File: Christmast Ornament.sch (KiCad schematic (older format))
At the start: 37 parts, among them J1 USB_OTG, J2 CONN_01X06, Q1 8205A, Q2 SI2302, SW1 SW_Push, SW2 SW_Push, U1 TP4056, U10 WS2812b, U2 HT7833, U3 DW01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

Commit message: Buzzer circuit and test points
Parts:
- added JP1: Jumper_NC_Dual, symbol Jumper_NC_Dual
- added Q3: BC817, TO_SOT_Packages_SMD:SOT-23, symbol BC817-40
- added R11: 470, Resistors_SMD:R_0805_HandSoldering, symbol R
- added R12, R13: 10K, Resistors_SMD:R_0805_HandSoldering, symbol R
- added TP1, TP2, TP3, TP4: TEST, Measurement_Points:Measurement_Point_Square-SMD-Pad_Small, symbol TEST
- D3: renamed from D?; footprint (none) -> Diodes_SMD:D_SMA_Handsoldering
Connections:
- net +3V3: now also JP1.1; no longer BZ1.1 (-), D3.1 (K)
- net BAT+: now also JP1.3, TP2.1
- net BAT-: now also TP4.1
- net Buzzer: now also R11.2
- net GND: now also Q3.2 (E), R12.2, R13.2, TP3.1
- net PIX_ON: now also R13.1
- net VCC: now also TP1.1
- net at BZ1.2 (+), D3.2 (A): now also Q3.3 (C)
- new net: BZ1.1 (-), D3.1 (K), JP1.2
- new net: Q3.1 (B), R11.1, R12.1
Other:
- note removed: "AÑADIR PUNTOS DE TEST"
- note removed: "Añadir puntos de test para conectar a bat+ o a 3.3v"
- note removed: "Revisar circuito para el zumbador.\n¿Añadir transistor, diodo, resistencia?"
- moved on the sheet: BZ1, C3, C6, D3, J2, Q2, R1, R5, R6, U10, U3, U4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

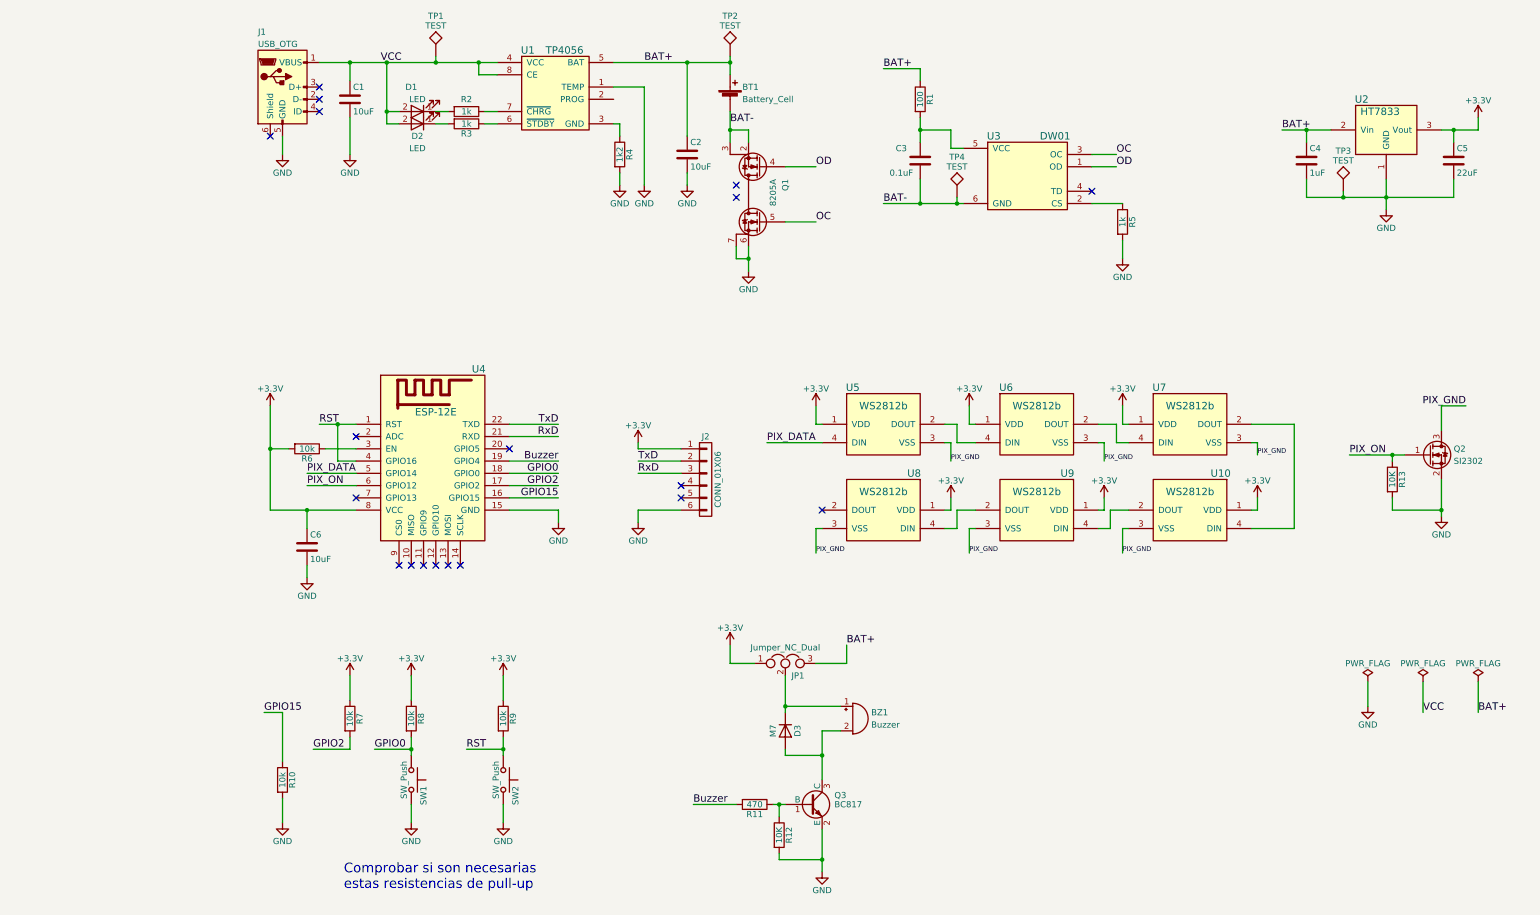
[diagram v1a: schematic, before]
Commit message: First attempt to distribute components
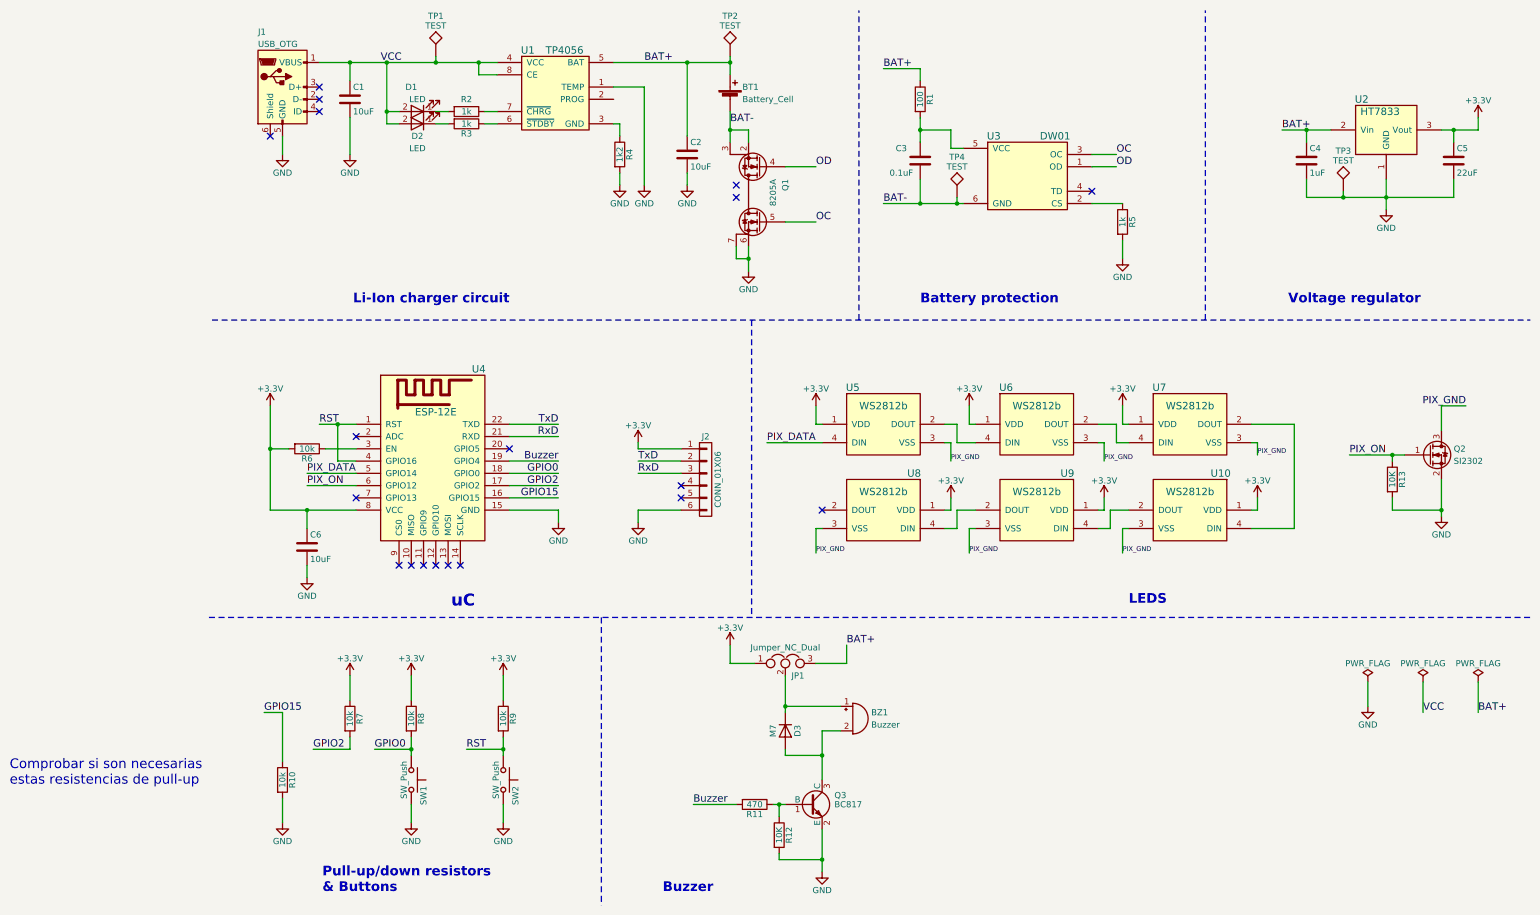
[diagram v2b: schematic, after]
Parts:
- BT1: footprint (none) -> MisModulos:18650_SMD_Case
- BZ1: footprint (none) -> MisModulos:Buzzer_8.5x8.5mm
- JP1: footprint (none) -> MisModulos:Jumper_2-NC
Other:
- note added: "Battery protection"
- note added: "Buzzer"
- note added: "LEDS"
- note added: "Li-Ion charger circuit"
- note added: "Pull-up/down resistors\n& Buttons"
- note added: "Voltage regulator"
- note added: "uC"
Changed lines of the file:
@@
 F 0 "BT1" H 4800 1300 50  0000 L CNN
 F 1 "Battery_Cell" H 4800 1200 50  0000 L CNN
-F 2 "" V 4700 1260 50  0001 C CNN
+F 2 "MisModulos:18650_SMD_Case" V 4700 1260 50  0001 C CNN
 F 3 "" V 4700 1260 50  0001 C CNN
 	1    4700 1200
@@
 F 0 "BZ1" H 5850 6300 50  0000 L CNN
 F 1 "Buzzer" H 5850 6200 50  0000 L CNN
-F 2 "" V 5675 6350 50  0001 C CNN
+F 2 "MisModulos:Buzzer_8.5x8.5mm" V 5675 6350 50  0001 C CNN
 F 3 "" V 5675 6350 50  0001 C CNN
 	1    5700 6250
@@
 	5150 6550 5450 6550
 Connection ~ 5450 6550
-Text Notes 1550 7650 0    79   ~ 0
+Text Notes -1175 6800 0    79   ~ 0
 Comprobar si son necesarias \nestas resistencias de pull-up
 $Comp
@@
 F 0 "JP1" H 5200 5700 50  0000 L CNN
 F 1 "Jumper_NC_Dual" H 5150 5900 50  0000 C BNN
-F 2 "" H 5150 5800 50  0001 C CNN
+F 2 "MisModulos:Jumper_2-NC" H 5150 5800 50  0001 C CNN
 F 3 "" H 5150 5800 50  0001 C CNN
 	1    5150 5800
@@
 	9700 1950 9700 2000
 Connection ~ 9700 2000
+Wire Notes Line
+	475  3000 11225 3000
+Wire Notes Line
+	5750 3000 5750 475
+Wire Notes Line
+	8575 3000 8575 475
+Wire Notes Line
+	450  5425 11225 5425
+Wire Notes Line
+	4875 3000 4875 5425
+Wire Notes Line
+	3650 5425 3650 7775
+Text Notes 1625 2875 0    79   ~ 16
+Li-Ion charger circuit
+Text Notes 6250 2875 0    79   ~ 16
+Battery protection
+Text Notes 9250 2875 0    79   ~ 16
+Voltage regulator
+Text Notes 7950 5325 0    79   ~ 16
+LEDS
+Text Notes 2425 5350 0    98   ~ 20
+uC
+Text Notes 4150 7675 0    79   ~ 16
+Buzzer
+Text Notes 1375 7675 0    79   ~ 16
+Pull-up/down resistors\n& Buttons
 $EndSCHEMATC

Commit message: PCB routed
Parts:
- added TP5, TP6: TEST, Measurement_Points:Measurement_Point_Square-SMD-Pad_Small, symbol TEST
- R4: value 1k2 -> 2k7
- renumbered U8 to U10, U10 to U8
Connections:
- net +3V3: now also J2.2 (P2), TP5.1; no longer J2.1 (P1)
- net GND: now also J2.1 (P1), TP6.1; no longer J2.6 (P6)
- net RxD: now also J2.5 (P5); no longer J2.3 (P3)
- net TxD: now also J2.3 (P3); no longer J2.2 (P2)

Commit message: PCB designed and gerbers
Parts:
- added C10, C11, C12, C7, C8, C9: 0.1uF, Capacitors_SMD:C_0805_HandSoldering, symbol C
- C5: value 22uF -> 2.2uF
- TP1: value TEST -> VCC
- TP2: renamed from TP6; value TEST -> GND
- TP3: renamed from TP2; value TEST -> BAT+
- TP4: value TEST -> BAT-
- TP5: value TEST -> 3V3
- TP6: renamed from TP3; value TEST -> GND
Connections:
- net +3V3: now also C10.1, C11.1, C12.1, C7.1, C8.1, C9.1
- net PIX_GND: now also C10.2, C11.2, C12.2, C7.2, C8.2, C9.2
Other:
- moved on the sheet: Q2, R13, U10, U5, U6, U7, U8, U9

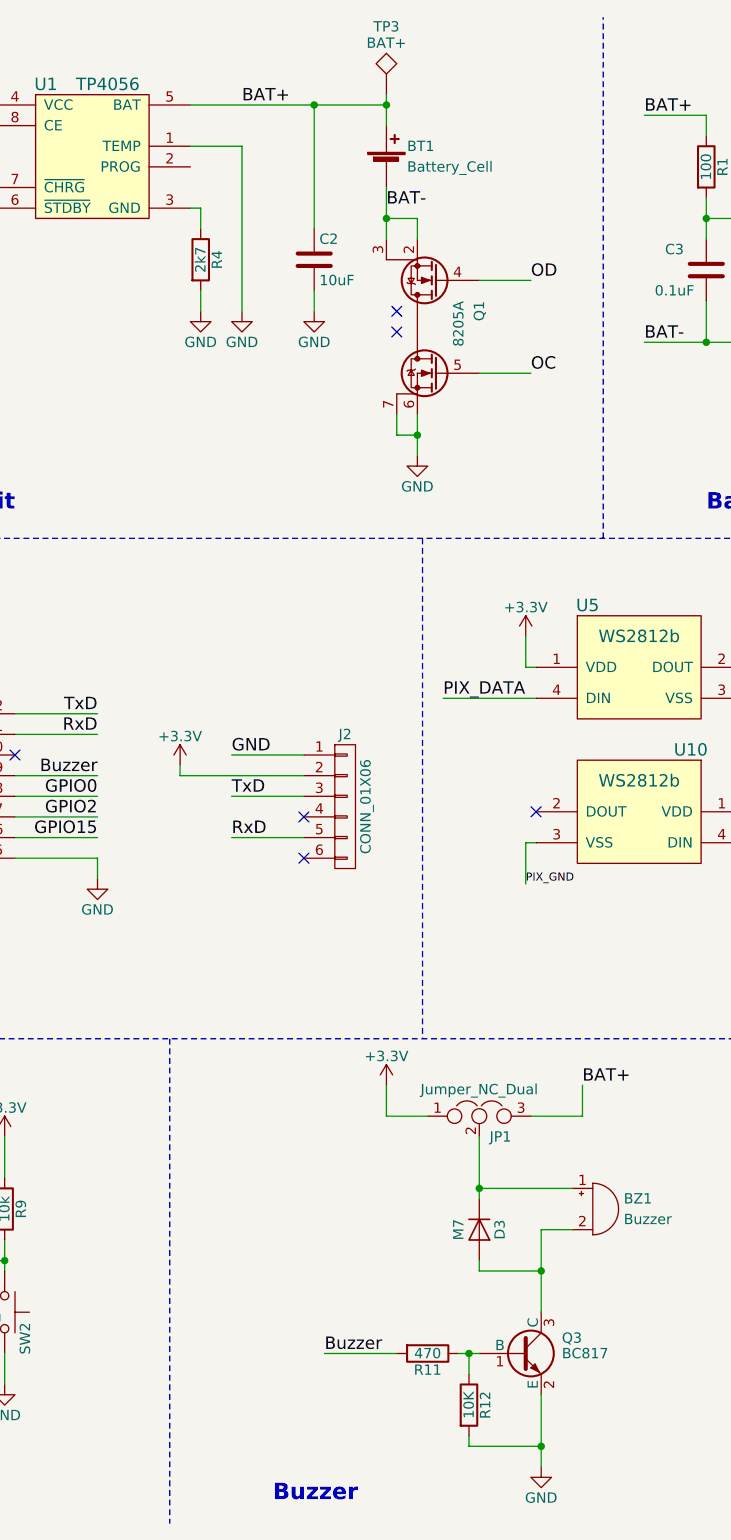
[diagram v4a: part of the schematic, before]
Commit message: TP4056 ground connection fixed
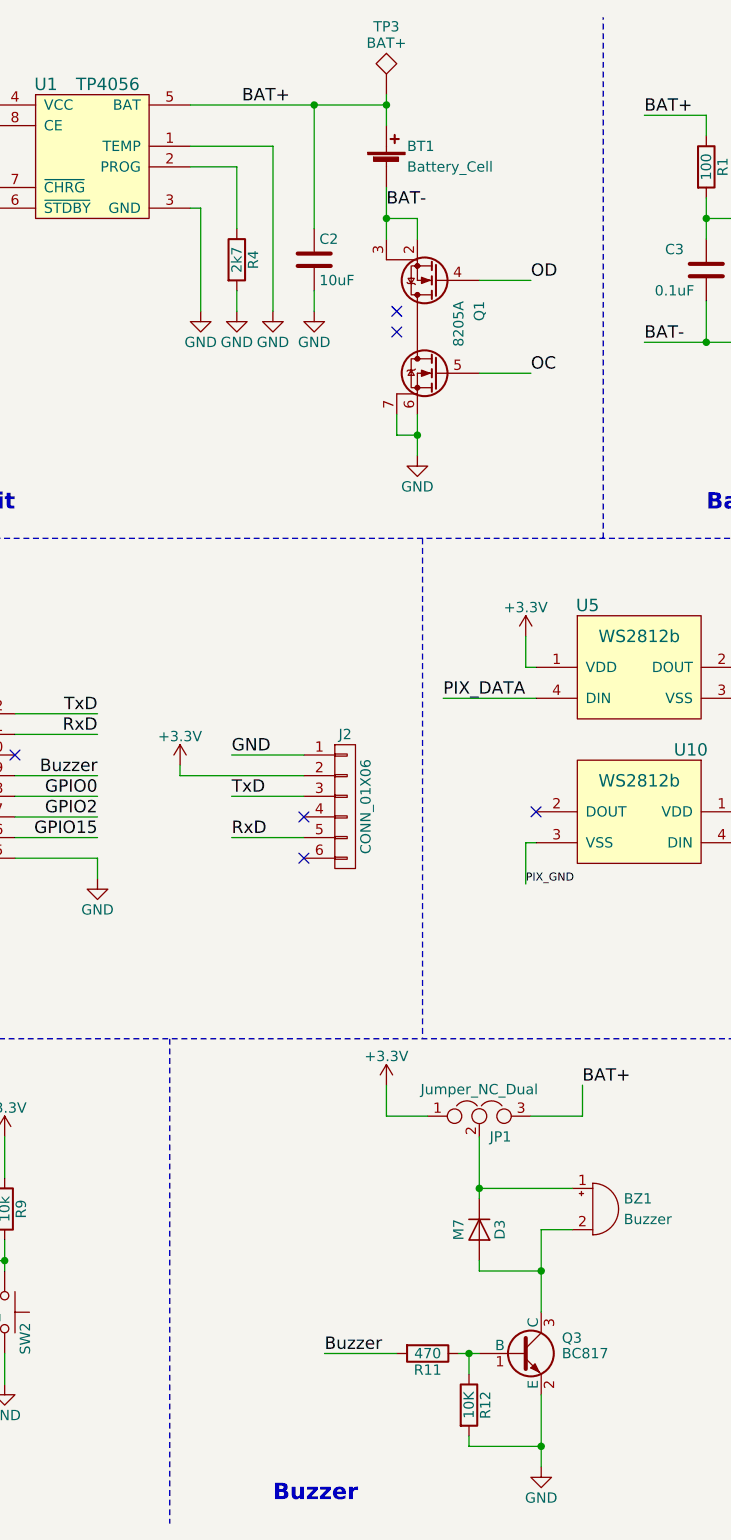
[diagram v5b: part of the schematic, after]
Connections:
- net GND: now also U1.3 (GND)
- net at U1.2 (PROG): now also R4.1
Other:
- moved on the sheet: R4
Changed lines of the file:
@@
 L GND #PWR01
 U 1 1 5AE440E5
-P 3800 1900
-F 0 "#PWR01" H 3800 1650 50  0001 C CNN
-F 1 "GND" H 3800 1750 50  0000 C CNN
-F 2 "" H 3800 1900 50  0001 C CNN
-F 3 "" H 3800 1900 50  0001 C CNN
-	1    3800 1900
+P 3975 1900
+F 0 "#PWR01" H 3975 1650 50  0001 C CNN
+F 1 "GND" H 3975 1750 50  0000 C CNN
+F 2 "" H 3975 1900 50  0001 C CNN
+F 3 "" H 3975 1900 50  0001 C CNN
+	1    3975 1900
 	1    0    0    -1
 $EndComp
@@
 L GND #PWR02
 U 1 1 5AE440FD
-P 4000 1900
-F 0 "#PWR02" H 4000 1650 50  0001 C CNN
-F 1 "GND" H 4000 1750 50  0000 C CNN
-F 2 "" H 4000 1900 50  0001 C CNN
-F 3 "" H 4000 1900 50  0001 C CNN
-	1    4000 1900
+P 4150 1900
+F 0 "#PWR02" H 4150 1650 50  0001 C CNN
+F 1 "GND" H 4150 1750 50  0000 C CNN
+F 2 "" H 4150 1900 50  0001 C CNN
+F 3 "" H 4150 1900 50  0001 C CNN
+	1    4150 1900
 	1    0    0    -1
 $EndComp
@@
 L R R4
 U 1 1 5AE4411E
-P 3800 1650
-F 0 "R4" V 3880 1650 50  0000 C CNN
-F 1 "2k7" V 3800 1650 50  0000 C CNN
-F 2 "Resistors_SMD:R_0805_HandSoldering" V 3730 1650 50  0001 C CNN
-F 3 "" H 3800 1650 50  0001 C CNN
-	1    3800 1650
+P 3975 1650
+F 0 "R4" V 4055 1650 50  0000 C CNN
+F 1 "2k7" V 3975 1650 50  0000 C CNN
+F 2 "Resistors_SMD:R_0805_HandSoldering" V 3905 1650 50  0001 C CNN
+F 3 "" H 3975 1650 50  0001 C CNN
+	1    3975 1650
 	1    0    0    -1
 $EndComp
@@
 	4700 1300 4700 1550
 Wire Wire Line
-	3750 1100 4000 1100
-Wire Wire Line
-	4000 1100 4000 1900
-Wire Wire Line
-	3750 1400 3800 1400
-Wire Wire Line
-	3800 1400 3800 1500
-Wire Wire Line
-	3800 1800 3800 1900
+	3975 1200 3975 1500
+Wire Wire Line
+	3975 1800 3975 1900
 Wire Wire Line
 	2800 1000 2650 1000
@@
 	4750 6950 4400 6950
 Wire Wire Line
-	5450 7500 5450 7150
+	5450 7150 5450 7500
 Wire Wire Line
 	5100 7050 5100 6950
@@
 	-1   0    0    -1
 $EndComp
+Wire Wire Line
+	4150 1100 4150 1900
+Wire Wire Line
+	3975 1200 3750 1200
+Wire Wire Line
+	3750 1100 4150 1100
+$Comp
+L GND #PWR?
+U 1 1 5B5777E2
+P 3800 1900
+F 0 "#PWR?" H 3800 1650 50  0001 C CNN
+F 1 "GND" H 3800 1750 50  0000 C CNN
+F 2 "" H 3800 1900 50  0001 C CNN
+F 3 "" H 3800 1900 50  0001 C CNN
+	1    3800 1900
+	1    0    0    -1
+$EndComp
+Wire Wire Line
+	3750 1400 3800 1400
+Wire Wire Line
+	3800 1400 3800 1900
 $EndSCHEMATC

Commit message: 8205A footprint changed
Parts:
- Q1: footprint Housings_SSOP:SSOP-8_2.95x2.8mm_Pitch0.65mm -> Housings_SSOP:TSSOP-8_4.4x3mm_Pitch0.65mm
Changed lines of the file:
@@
 F 0 "Q1" H 5450 1550 50  0000 L CNN
 F 1 "8205A" H 5450 1450 50  0000 L CNN
-F 2 "Housings_SSOP:SSOP-8_2.95x2.8mm_Pitch0.65mm" H 5500 950 50  0001 L CIN
+F 2 "Housings_SSOP:TSSOP-8_4.4x3mm_Pitch0.65mm" H 5500 950 50  0001 L CIN
 F 3 "" V 5350 1350 50  0001 L CNN
 	1    5150 1550
@@
 	3750 1100 4150 1100
 $Comp
-L GND #PWR?
+L GND #PWR035
 U 1 1 5B5777E2
 P 3800 1900
-F 0 "#PWR?" H 3800 1650 50  0001 C CNN
+F 0 "#PWR035" H 3800 1650 50  0001 C CNN
 F 1 "GND" H 3800 1750 50  0000 C CNN
 F 2 "" H 3800 1900 50  0001 C CNN
